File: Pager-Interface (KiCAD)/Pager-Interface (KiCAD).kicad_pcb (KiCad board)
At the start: 2 copper layers, 100 x 35 mm, 22 parts, among them J1 USB_B_Micro, J2 SMA ANT, Q1 BC817, Q2 BC817, U1 AMS1117-3.3, U2 CP2102N-A01-GQFN24, U3 SI4432-Module, U4 ESP32-WROOM

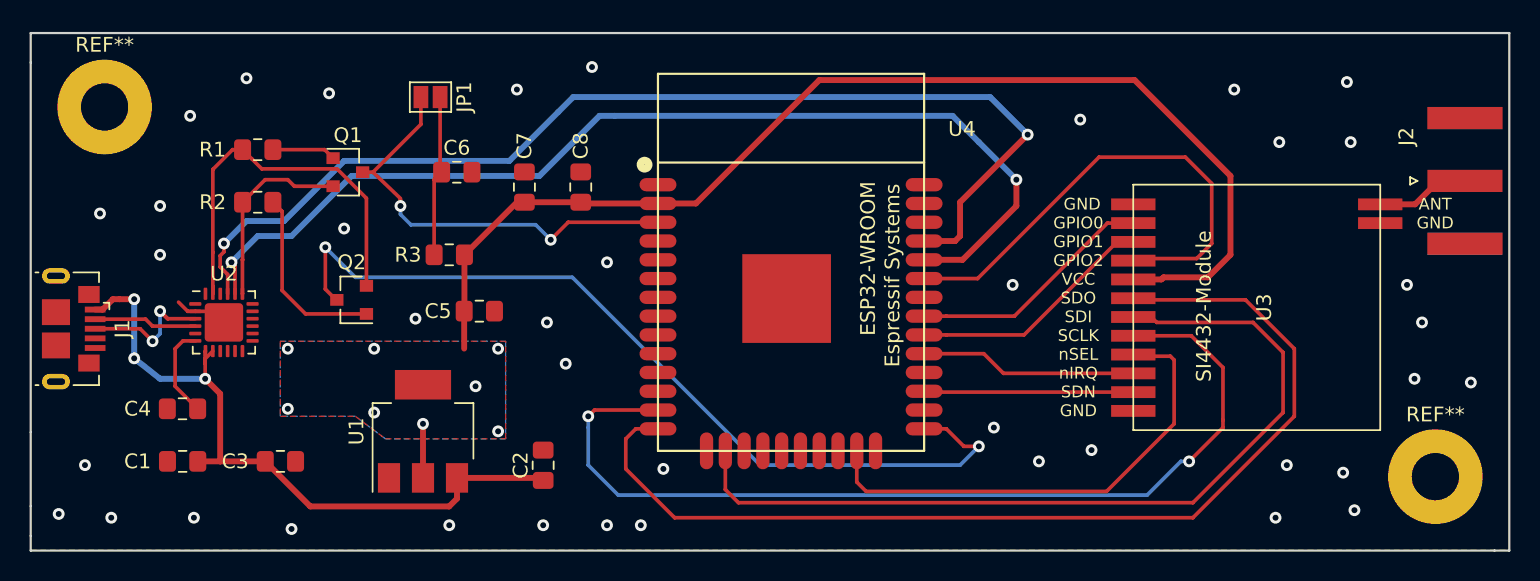
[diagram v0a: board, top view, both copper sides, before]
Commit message: changed part numbers -> cp2102 to gqfn28 footprint + created outputfile for jlcpcb + some more silk text
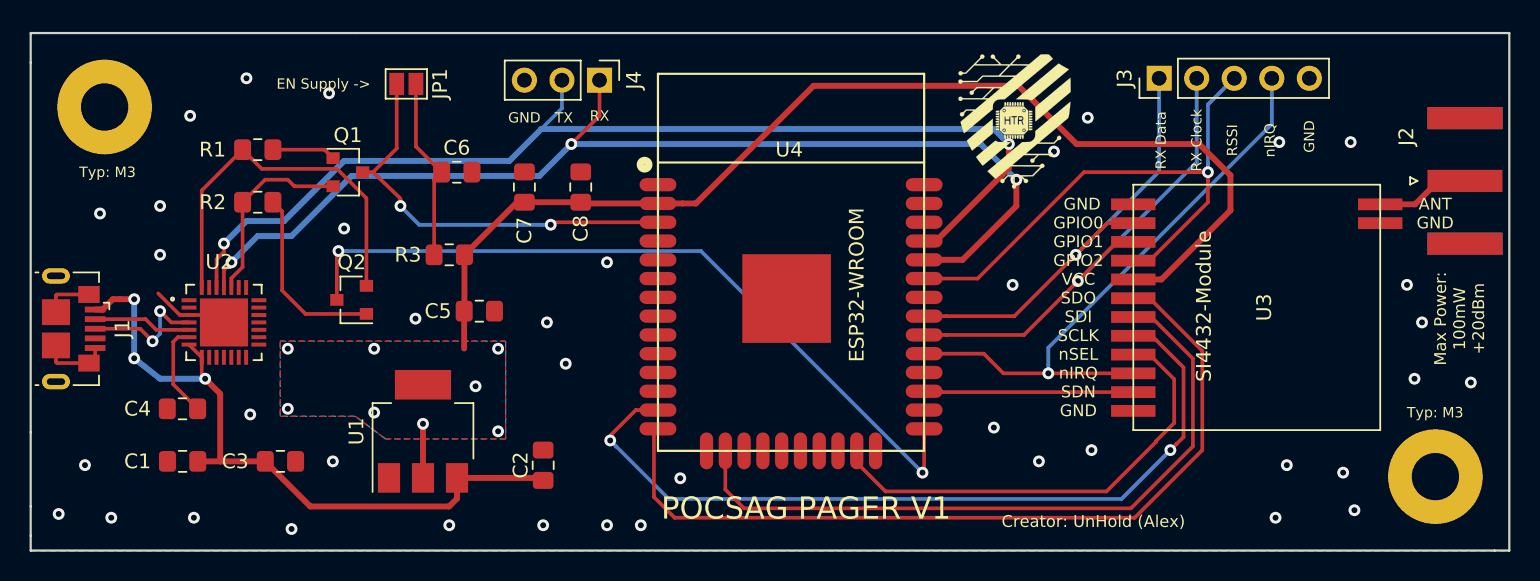
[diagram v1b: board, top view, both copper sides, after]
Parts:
- added G***: LOGO, HTR:HTR_Logo, F.Cu at (105.5, 102.0)
- added J3: Debug SI4432, Connector_PinHeader_2.54mm:PinHeader_1x05_P2.54mm_Vertical, F.Cu at (115.3, 99.1)
- added J4: UART, Connector_PinHeader_2.54mm:PinHeader_1x03_P2.54mm_Vertical, F.Cu at (77.5, 99.2)
- U2: value CP2102N-A01-GQFN24 -> CP2102N-A01-GQFN28; footprint Package_DFN_QFN:QFN-24-1EP_4x4mm_P0.5mm_EP2.6x2.6mm -> CP2102:CP2102-GQFN28
- moved JP1 1.86 mm to (64.4, 99.4)
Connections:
- J1 pad 2: Net-(J1-Pad2) -> /D-
- J1 pad 3: Net-(J1-Pad3) -> /D+
- Q1 pad 2: Net-(Q1-Pad2) -> /RST
- Q2 pad 2: Net-(Q2-Pad2) -> /DTR
- R1 pad 2: Net-(Q2-Pad2) -> /DTR
- R2 pad 2: Net-(Q1-Pad2) -> /RST
- U2 pad 10: Net-(U2-Pad10) -> (no net)
- U2 pad 19: Net-(Q1-Pad2) -> Net-(U2-Pad19)
- U2 pad 2: GND -> Net-(U2-Pad2)
- U2 pad 20: /RX0 -> Net-(U2-Pad20)
- U2 pad 21: /TX0 -> Net-(U2-Pad21)
- U2 pad 23: Net-(Q2-Pad2) -> Net-(U2-Pad23)
- U2 pad 24: Net-(U2-Pad24) -> /RST
- U2 pad 25: GND -> /RX0
- U2 pad 3: Net-(J1-Pad3) -> GND
- U2 pad 4: Net-(J1-Pad2) -> /D+
- U2 pad 5: Net-(U2-Pad5) -> /D-
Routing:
- net Net-(Q2-Pad2): track 27.1 -> 0.00 mm
- net /nIRQ: track 14.7 -> 40.9 mm, vias 0 -> 1
- net /DTR: track 0.00 -> 26.1 mm
- net /RX_Clock: track 16.8 -> 33.8 mm, vias 0 -> 1
- net /RX_Data: track 16.8 -> 31.0 mm, vias 0 -> 1
- net /MISO: track 70.8 -> 57.1 mm
- net Net-(Q1-Pad2): track 13.1 -> 0.00 mm
- net /RST: track 0.00 -> 13.0 mm
- net /MOSI: track 58.4 -> 47.6 mm
- net Net-(J1-Pad3): track 9.79 -> 0.00 mm, vias 2 -> 0
- net GND: track 3.64 -> 13.2 mm, vias 40 -> 39
- net /CLK: track 64.9 -> 55.4 mm
- net /D+: track 0.00 -> 8.75 mm, vias 0 -> 2
- net Net-(J1-Pad2): track 6.97 -> 0.00 mm
- net /IO0: track 58.9 -> 52.1 mm
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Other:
- board text added: "Creator: UnHold (Alex)"
- board text added: "EN Supply ->"
- board text added: "GND"
- board text added: "Max Power: 100mW +20dBm"
- board text added: "POCSAG PAGER V1"
- board text added: "RSSI"
- board text added: "RX"
- board text added: "RX Clock"
- board text added: "RX Data"
- board text added: "TX"
- board text added: "Typ: M3"
- board text added: "nIRQ"

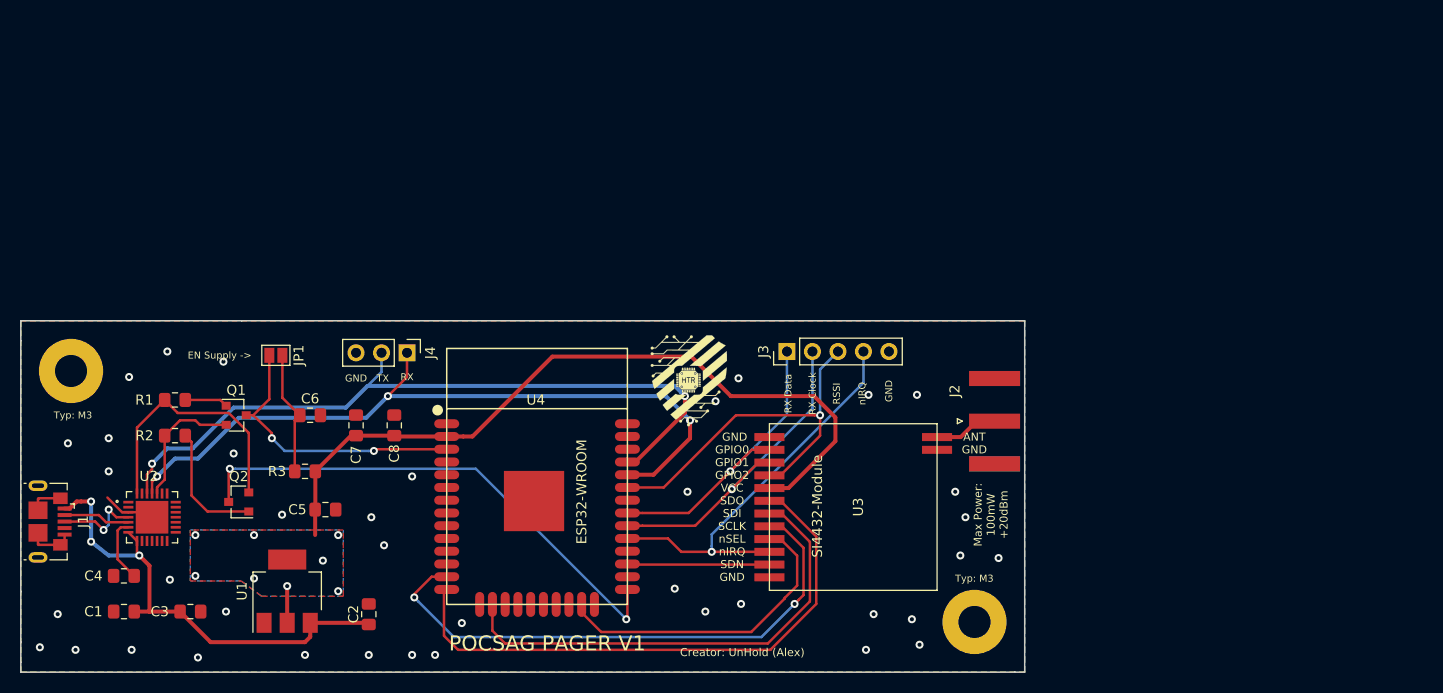
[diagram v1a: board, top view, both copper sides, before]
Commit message: Changed the PCB to use the NodeMCU, because it is just a prototype and won't be used in the future
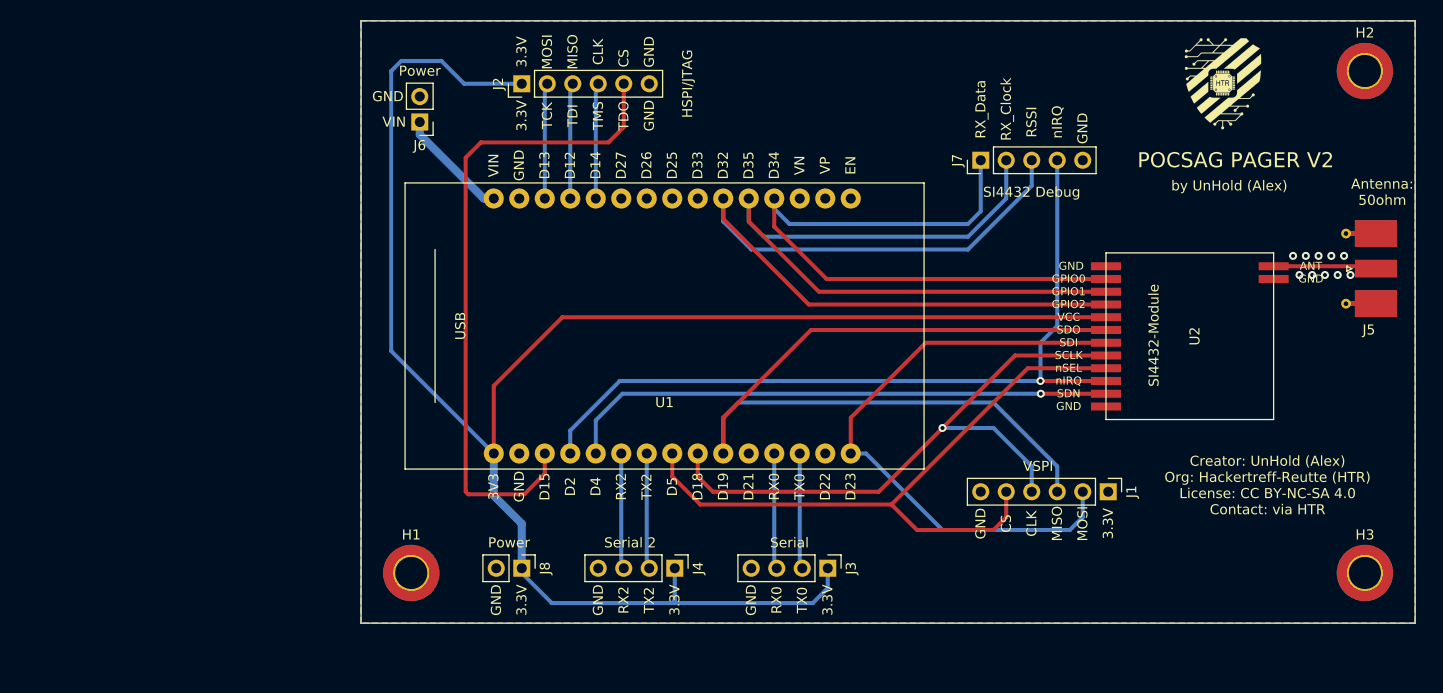
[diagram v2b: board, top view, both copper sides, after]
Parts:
- removed C1, C4, C8: 100nF, Capacitor_SMD:C_0805_2012Metric_Pad1.15x1.40mm_HandSolder
- removed C2, C5, C7: 10uF, Capacitor_SMD:C_0805_2012Metric_Pad1.15x1.40mm_HandSolder
- removed C3: 4.7uF, Capacitor_SMD:C_0805_2012Metric_Pad1.15x1.40mm_HandSolder
- removed C6: 1uF, Capacitor_SMD:C_0805_2012Metric_Pad1.15x1.40mm_HandSolder
- removed the G*** at (105.5, 102.0)
- removed JP1: EN Supply, Jumper:SolderJumper-2_P1.3mm_Open_Pad1.0x1.5mm
- removed Q1, Q2: BC817, Package_TO_SOT_SMD:SOT-23
- removed R1, R2, R3: 10k, Resistor_SMD:R_0805_2012Metric_Pad1.15x1.40mm_HandSolder
- removed REF** (x2): MountingHole_3.2mm_M3_Pad, MountingHole:MountingHole_3.2mm_M3_Pad
- removed U3: SI4432-Module, SI4432 Module:SI4432-Module
- removed U4: ESP32-WROOM, ESP32:ESP32-WROOM
- added G***: LOGO, Pager-Interface (KiCAD):Ham-Radio, F.Cu at (128.3, 102.9)
- added G***: LOGO, Pager-Interface (KiCAD):HTR_Logo, F.Cu at (158.8, 72.4)
- added H1: M3, MountingHole:MountingHole_3.2mm_M3_DIN965_Pad_TopBottom, F.Cu at (77.9, 121.1)
- added H2: M3, MountingHole:MountingHole_3.2mm_M3_DIN965_Pad_TopBottom, F.Cu at (172.9, 71.1)
- added H3: M3, MountingHole:MountingHole_3.2mm_M3_DIN965_Pad_TopBottom, F.Cu at (172.9, 121.1)
- added J5: SMA ANT, Connector_Coaxial:SMA_Molex_73251-2120_EdgeMount_Horizontal, F.Cu at (174.0, 90.8)
- added J6: Ext Power, Connector_PinHeader_2.54mm:PinHeader_1x02_P2.54mm_Vertical, F.Cu at (78.7, 76.2)
- added J7: Debug SI4432, Connector_PinHeader_2.54mm:PinHeader_1x05_P2.54mm_Vertical, F.Cu at (134.6, 80.0)
- added J8: Power, Connector_PinHeader_2.54mm:PinHeader_1x02_P2.54mm_Vertical, F.Cu at (88.9, 120.7)
- J1: value USB_B_Micro -> VSPI; footprint Connector_USB:USB_Micro-B_GCT_USB3076-30-A -> Connector_PinHeader_2.54mm:PinHeader_1x06_P2.54mm_Vertical
- J2: value SMA ANT -> HSPI; footprint Connector_Coaxial:SMA_Amphenol_132289_EdgeMount -> Connector_PinHeader_2.54mm:PinHeader_1x06_P2.54mm_Vertical
- J3: value Debug SI4432 -> Serial; footprint Connector_PinHeader_2.54mm:PinHeader_1x05_P2.54mm_Vertical -> Connector_PinHeader_2.54mm:PinHeader_1x04_P2.54mm_Vertical
- J4: value UART -> Serial2; footprint Connector_PinHeader_2.54mm:PinHeader_1x03_P2.54mm_Vertical -> Connector_PinHeader_2.54mm:PinHeader_1x04_P2.54mm_Vertical
- U1: value AMS1117-3.3 -> ESP32_NodeMCU; footprint Package_TO_SOT_SMD:SOT-223-3_TabPin2 -> Pager-Interface (KiCAD):ESP32_NodeMCU
- U2: value CP2102N-A01-GQFN28 -> SI4432-Module; footprint CP2102:CP2102-GQFN28 -> Pager-Interface (KiCAD):SI4432-Module
- moved J1 105.5 mm to (147.3, 113.0)
- moved U2 104.9 mm to (155.4, 97.5), turned to 90 degrees
- moved J2 57.9 mm to (88.9, 72.4), turned to 90 degrees
- moved U1 45.9 mm to (103.1, 96.5), turned to 180 degrees
- moved J4 34.2 mm to (104.1, 120.7)
- moved J3 22.0 mm to (119.4, 120.7), turned to 270 degrees
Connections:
- J1 pad 1: +5V -> +3V3
- J1 pad 2: /D- -> /VSPI_MOSI
- J1 pad 3: /D+ -> /VSPI_MISO
- J1 pad 4: Net-(J1-Pad4) -> /VSPI_CLK
- J1 pad 5: GND -> /VSPI_CS
- J2 pad 1: Net-(J2-Pad1) -> +3V3
- J2 pad 2: GND -> /HSPI_MOSI
- J3 pad 1: /RX_Data -> +3V3
- J3 pad 2: /RX_Clock -> /TX0
- J3 pad 3: /RSSI -> /RX0
- J3 pad 4: /nIRQ -> GND
- J4 pad 1: /RX0 -> +3V3
- J4 pad 2: /TX0 -> /TX2
- J4 pad 3: GND -> /RX2
- U1 pad 1: GND -> /VSPI_MOSI
- U1 pad 2: +3V3 -> Net-(U1-Pad2)
- U1 pad 3: +5V -> /TX0
- U2 pad 1: Net-(U2-Pad1) -> GND
- U2 pad 10: (no net) -> /nIRQ
- U2 pad 11: Net-(U2-Pad11) -> /SDN
- U2 pad 12: Net-(U2-Pad12) -> GND
- U2 pad 14: Net-(U2-Pad14) -> GND
- U2 pad 2: Net-(U2-Pad2) -> /RX_Data
- U2 pad 3: GND -> /RX_Clock
- U2 pad 4: /D+ -> /RSSI
- U2 pad 5: /D- -> +3V3
- U2 pad 6: Net-(C4-Pad1) -> /VSPI_MISO
- U2 pad 7: +5V -> /VSPI_MOSI
- U2 pad 8: +5V -> /VSPI_CLK
- U2 pad 9: Net-(U2-Pad9) -> /VSPI_CS
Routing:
- net +3V3: track 80.1 -> 178.2 mm, vias 8 -> 0
- net /VSPI_MISO: track 0.00 -> 87.9 mm
- net /VSPI_CS: track 0.00 -> 67.8 mm
- net /HSPI_CS: track 0.00 -> 65.5 mm
- net /RX0: track 74.7 -> 11.5 mm, vias 3 -> 0
- net /VSPI_CLK: track 0.00 -> 62.2 mm, vias 0 -> 1
- net /TX0: track 73.2 -> 11.5 mm, vias 2 -> 0
- net /VSPI_MOSI: track 0.00 -> 61.4 mm
- net /MISO: track 57.1 -> 0.00 mm
- net /CLK: track 55.4 -> 0.00 mm, vias 2 -> 0
- net /IO0: track 52.1 -> 0.00 mm, vias 2 -> 0
- net /MOSI: track 47.6 -> 0.00 mm
- net +5V: track 47.3 -> 0.00 mm, vias 3 -> 0
- net /RSSI: track 38.0 -> 83.0 mm, vias 1 -> 0
- net /SDN: track 14.2 -> 55.2 mm, vias 0 -> 1
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- removed copper zone on B.Cu, net +3V3
- removed copper zone on F.Cu, net +3V3
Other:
- board size 100 x 35 mm -> 105 x 60 mm
- board text added: "3.3V"
- board text added: "Antenna: 50ohm"
- board text added: "CLK"
- board text added: "CS"
- board text added: "Creator: UnHold (Alex) Org: Hackertreff-Reutte (HTR) License: CC BY-NC-SA 4.0 Contact: via HTR"
- board text added: "HSPI/JTAG"
- board text added: "MISO"
- board text added: "MOSI"
- board text added: "POCSAG PAGER V2"
- board text added: "Power"
- board text added: "RX0"
- board text added: "RX2"
- board text added: "RX_Clock"
- board text added: "RX_Data"
- board text added: "SI4432 Debug"
- board text added: "Serial"
- board text added: "Serial 2"
- board text added: "TCK"
- board text added: "TDI"
- board text added: "TDO"
- board text added: "TMS"
- board text added: "TX0"
- board text added: "TX2"
- board text added: "VIN"
- board text added: "VSPI"
- board text added: "by UnHold (Alex)"
- board text removed: "Creator: UnHold (Alex)"
- board text removed: "EN Supply ->"
- board text removed: "Max Power: 100mW +20dBm"
- board text removed: "POCSAG PAGER V1"
- board text removed: "RX"
- board text removed: "RX Clock"
- board text removed: "RX Data"
- board text removed: "TX"
- board text removed: "Typ: M3"
